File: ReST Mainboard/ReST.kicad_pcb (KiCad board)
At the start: 2 copper layers, 100 x 100 mm, 368 parts, among them P20 CONN_02X04, P21 CONN_02X04, P24 CONN_01X03, P26 CONN_01X03, P28 CONN_01X03, P30 CONN_01X03, P32 CONN_01X03, P34 CONN_01X03, P35 SCREW_01X04, P36 SCREW_01X04, P37 SCREW_01X04, P38 SCREW_01X04, P5 USB_OTG, P9 CONN_01X02, U2 USBLC6-2, U4 LM2574N-ADJ

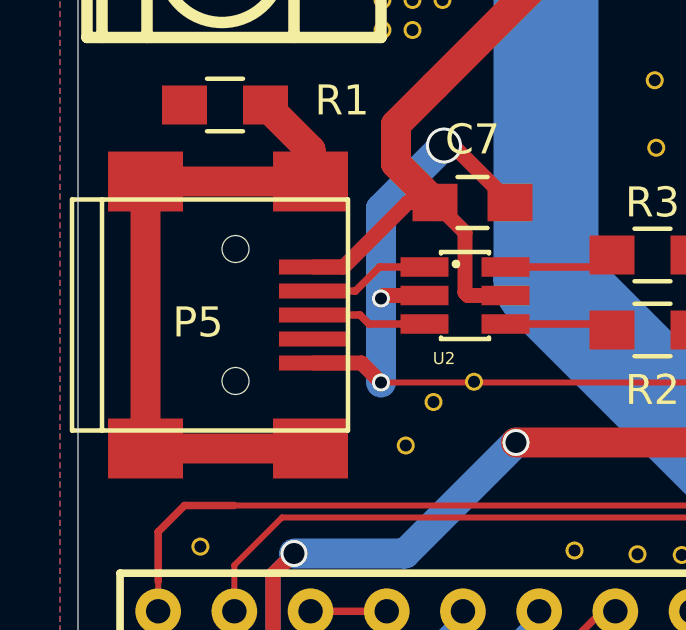
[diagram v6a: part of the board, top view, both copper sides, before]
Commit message: Finished Combined PCB and Gerber files
Combined pcb fits on 10x10cm, breakable and gerbers are finished for elecrow order. will order everything this weekend, lets see if it works.
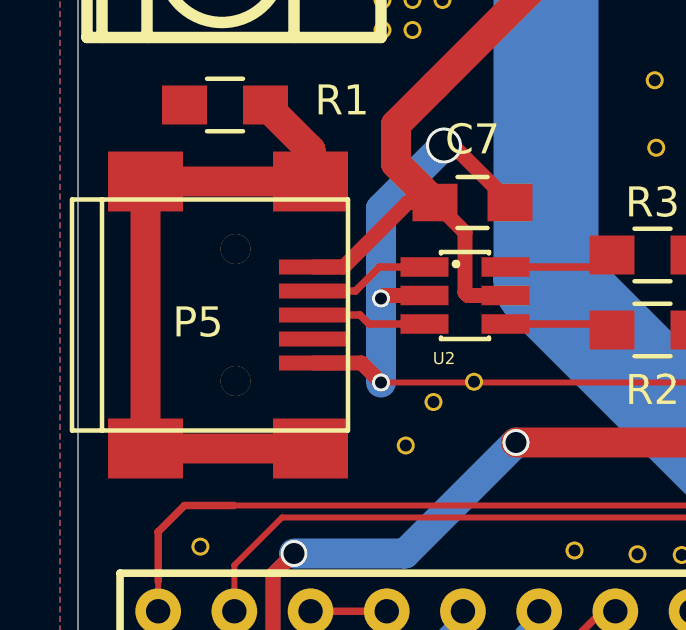
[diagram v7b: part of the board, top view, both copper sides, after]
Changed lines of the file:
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@@
   )
   (setup
-    (last_trace_width 0.5)
+    (last_trace_width 0.25)
     (user_trace_width 0.2)
     (user_trace_width 0.3)
@@
     (mod_text_size 1 1)
     (mod_text_width 0.15)
-    (pad_size 0.6 0.6)
-    (pad_drill 0.4)
+    (pad_size 1 1)
+    (pad_drill 1)
     (pad_to_mask_clearance 0.2)
     (aux_axis_origin 0 0)
@@
     (visible_elements 7FFFFF7F)
     (pcbplotparams
-      (layerselection 0x010f0_80000001)
+      (layerselection 0x000f0_80000001)
       (usegerberextensions true)
-      (excludeedgelayer true)
+      (usegerberattributes true)
+      (excludeedgelayer false)
       (linewidth 0.100000)
       (plotframeref false)
@@
     (pad 6 smd rect (at -2.14884 4.45008) (size 2.49936 1.99898) (layers F.Cu F.Paste F.Mask)
       (net 118 "Net-(P5-Pad6)"))
-    (pad "" np_thru_hole circle (at 0.8509 -2.19964) (size 0.89916 0.89916) (drill 0.89916) (layers *.Cu *.Mask F.SilkS))
-    (pad "" np_thru_hole circle (at 0.8509 2.19964) (size 0.89916 0.89916) (drill 0.89916) (layers *.Cu *.Mask F.SilkS))
+    (pad "" thru_hole circle (at 0.8509 -2.19964) (size 1 1) (drill 1) (layers *.Cu *.Mask F.SilkS))
+    (pad "" thru_hole circle (at 0.8509 2.19964) (size 1 1) (drill 1) (layers *.Cu *.Mask F.SilkS))
     (model ../../../../../../Users/Matjas/Documents/Git/RepRapSTM32duinoDriver/3D-Models/conn_pc/usb_B_mini_smd.wrl
       (at (xyz -0.025 0 0))

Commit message: Mainboard structure made and most modules finished
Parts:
- removed ?: , Pin_Headers:Pin_Header_Straight_1x04
- removed GND (x3), REF**11, REF**111 (x3), REF**11101, REF**1111 (x2), REF**11111 (x2), REF**111111, REF**111112, REF**111113, REF**111114, REF**111115, REF**111116, REF**11112, REF**111121, REF**111122, REF**111123, REF**111124, REF**111125, REF**111126, REF**11113, REF**111131, REF**111132, REF**111133, REF**111134, REF**111135, REF**111136, REF**11114, REF**111141, REF**111142, REF**111143, REF**111144, REF**111145, REF**111146, REF**11115, REF**111151, REF**111152, REF**111153, REF**111154, REF**111155, REF**111156, REF**11116, REF**1112, REF**11121 (x2), REF**11122, REF**11123, REF**11124, REF**11125, REF**11126, REF**1113, REF**1114, REF**1115, REF**1116, REF**112 (x2), REF**1121 (x2), REF**1122, REF**1123, REF**1124, REF**1125, REF**1126, REF**113 (x2), REF**1131 (x2), REF**1132, REF**1133, REF**1134, REF**1135, REF**1136, REF**114 (x2), REF**1141, REF**115 (x2), REF**1151, REF**116 (x2), REF**1161, REF**1171, REF**1181, REF**1191, REF**12, REF**121 (x3), REF**122 (x2), REF**123 (x2), REF**124 (x2), REF**125 (x2), REF**126 (x2), REF**131 (x5), REF**131111 (x6), REF**131112, REF**131113, REF**131114, REF**131115, REF**131121, REF**131122, REF**131123, REF**131124, REF**131125, REF**131131, REF**131132, REF**131133, REF**131134, REF**131135, REF**131141, REF**131142, REF**131143, REF**131144, REF**131145, REF**131151, REF**131152, REF**131153, REF**131154, REF**131155, REF**132 (x2), REF**133 (x2), REF**134 (x2), REF**135 (x2), REF**136, REF**141 (x2), REF**142, REF**143, REF**144, REF**145, REF**146, REF**21, REF**22, REF**31 (x58), REF**311 (x3), REF**3111 (x3), REF**3112 (x2), REF**3113, REF**312 (x3), REF**3121 (x3), REF**3122 (x2), REF**313 (x10), REF**3131 (x2), REF**3132, REF**3141 (x2), REF**3142, REF**3151 (x2), REF**3152, REF**3161, REF**32, REF**321 (x3), REF**322 (x3), REF**323 (x3), REF**331 (x2), REF**332 (x3), REF**333 (x3), REF**341, REF**342, REF**343: VIA-0.6mm, ReST-Library:VIA-0.6mm
- removed GND: , ReST-Library:VIA-0.6mm
- removed P20: CONN_02X04, ReST-Library:Pin_Header_Angled_2x04
- removed P22: , Pin_Headers:Pin_Header_Straight_1x03
- removed P25: , 2:mpt_0,5%2f6-2,54
- removed P26, P30, P32: CONN_01X03, Pin_Headers:Pin_Header_Straight_1x03
- removed R6: 2K7, Resistors_SMD:R_0805_HandSoldering
- removed R7: 1K6, Resistors_SMD:R_0805_HandSoldering
- added P11: CONN_01X04, Pin_Headers:Pin_Header_Straight_1x04, F.Cu at (197.2, 106.8)
- C1, C2, C3, C4, C5, C6, C9: value (none) -> 100nF
- C12: value 22uF -> 10uF; footprint ReST-Library:CP-PANASONIC-SMT_D -> Capacitors_SMD:C_0805_HandSoldering
- C13: value 220uF -> 10uF; footprint ReST-Library:CP-PANASONIC-SMT_D -> Capacitors_SMD:C_0805_HandSoldering
- C14, C15, C16, C17, C18, C19: value (none) -> 10nF
- C24, C25: value (none) -> 30pF
- C7: footprint Capacitors_SMD:C_0805_HandSoldering -> Capacitors_SMD:C_0603_HandSoldering
- C8: value (none) -> 10uF
- D1: value 1N5819 -> 1N400x; footprint ReST-Library:DO-214AC(SMA) -> ReST-Library:DO-214AC.SMA
- F1: footprint ReST-Library:JEF-703C -> ReST-Library:MINI-FUSE
- IC1: value (none) -> AT24C128
- L1: value (none) -> BEAD
- L2: value 330uH -> 2.2uH; footprint Inductors:SELF-WE-PD-XXL -> ReST-Library:CD32
- P1, P2: value (none) -> CONN_01X03; footprint ReST-Library:Pin_Header_Angled_2x08 -> Pin_Headers:Pin_Header_Straight_1x03
- P10, P19, P40, P41, P42: value (none) -> CONN_01X04
- P12: value (none) -> CONN_02X03; footprint Pin_Headers:Pin_Header_Straight_2x04 -> Pin_Headers:Pin_Header_Straight_2x03
- P13: value (none) -> CONN_02X04; footprint Pin_Headers:Pin_Header_Straight_1x03 -> ReST-Library:REST_STEPPER
- P14: value (none) -> CONN_02X03
- P15: value (none) -> CONN_02X04; footprint Pin_Headers:Pin_Header_Straight_1x05 -> ReST-Library:REST_STEPPER
- P16: value (none) -> CONN_02X06; footprint Pin_Headers:Pin_Header_Straight_1x03 -> ReST-Library:REST_ADDITIONAL
- P17: value (none) -> CONN_02X03; footprint Pin_Headers:Pin_Header_Straight_1x04 -> ReST-Library:REST_HEATBED
- P18, P39: value (none) -> CONN_02X04
- P23: value (none) -> CONN_02X07; footprint 2:mpt_0,5%2f6-2,54 -> ReST-Library:REST_HEATER
- P24: value CONN_01X03 -> CONN_02X07; footprint Pin_Headers:Pin_Header_Straight_1x03 -> ReST-Library:REST_HEATER
- P27: value (none) -> CONN_02X06; footprint 2:mpt_0,5%2f6-2,54 -> Pin_Headers:Pin_Header_Straight_2x06
- P3: value (none) -> CONN_01X03; footprint ReST-Library:Pin_Header_Angled_2x07 -> Pin_Headers:Pin_Header_Straight_1x03
- P35, P36, P37, P38: footprint 2:mpt_0,5%2f4-2,54 -> ReST-Library:pt_1,5-4-3,5-h
- P4: value (none) -> CONN_01X03; footprint ReST-Library:Pin_Header_Angled_2x10 -> Pin_Headers:Pin_Header_Straight_1x03
- P43, P44, P45, P46: value (none) -> CONN_02X03; footprint Pin_Headers:Pin_Header_Straight_2x03 -> ReST-Library:bb02-hp06
- P6, P7: value (none) -> CONN_02X05
- P8: value (none) -> CONN_01X03; footprint Pin_Headers:Pin_Header_Straight_1x09 -> Pin_Headers:Pin_Header_Straight_1x03
- P9: footprint 5mm-pitch-terminal:mkds_1,5-2 -> ReST-Library:screw-5-2P
- R10, R11, R8, R9: value (none) -> 100K
- R12, R13: value (none) -> 4K7
- R2, R3: footprint Resistors_SMD:R_0805_HandSoldering -> Resistors_SMD:R_0603_HandSoldering
- R5: value (none) -> 10K
- SW1: value (none) -> SW-SPST-NO
- U1: value (none) -> STM32F103VE; footprint Housings_QFP:TQFP-100_14x14mm_Pitch0.5mm -> ReST-Library:LQFP100-14x14
- U3: value (none) -> L7805ACD2T-TR
- U4: value LM2574N-ADJ -> LM3671MFX-3.3; footprint Housings_DIP:DIP-8_W7.62mm_LongPads -> TO_SOT_Packages_SMD:SOT-23-5
- U5, U6, U7, U8: value (none) -> POLOLU_A4988
- X1: value (none) -> Crystal_Small; footprint Crystals:Crystal_HC49-SD_SMD -> ReST-Library:2P-5032
- moved P2 197.0 mm to (191.3, 152.5), turned to 180 degrees
- moved P1 181.9 mm to (196.4, 152.5), turned to 180 degrees
- moved P3 161.6 mm to (193.8, 152.5), turned to 180 degrees
- moved P16 148.8 mm to (173.4, 144.7), turned to 180 degrees
- moved P4 148.1 mm to (188.7, 152.5), turned to 180 degrees
- moved P19 146.8 mm to (197.2, 110.2), turned to 270 degrees
- moved P10 142.7 mm to (197.2, 103.1), turned to 270 degrees
- moved P15 139.9 mm to (189.9, 71.5), turned to 0 degrees
- moved P6 137.1 mm to (197.2, 126.2), turned to 270 degrees
- moved P39 133.6 mm to (161.3, 141.7), turned to 270 degrees
- moved P7 130.2 mm to (197.2, 132.2), turned to 270 degrees
- moved P35 127.0 mm to (157.5, 149.7)
- moved P45 126.6 mm to (157.0, 126.3), turned to 90 degrees
- moved U7 126.3 mm to (157.5, 129.8), turned to 270 degrees
- moved R11 123.4 mm to (157.5, 131.6), turned to 180 degrees
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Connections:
- net Net-(C2-Pad2) renamed /RESET
- C10 pad 1: GND -> +12V
- C10 pad 2: +12V -> GND
- C11 pad 1: GND -> VEE
- C11 pad 2: VCC/2 -> GND
- C12 pad 1: VAA -> GND
- C12 pad 2: GND -> +5V
- C13 pad 1: +3V3 -> GND
- C13 pad 2: GND -> +3V3
- D1 pad 1: Net-(D1-Pad1) -> +12V
- L2 pad 1: Net-(D1-Pad1) -> Net-(L2-Pad1)
- P1 pad 1: +12V -> +3V3
- P1 pad 3: +12V -> /X-MIN
- P12 pad 1: +5V -> /SERVO1
- P12 pad 2: GND -> /SERVO2
- P12 pad 4: GND -> +5V
- P12 pad 5: +5V -> GND
- P13 pad 1: +12V -> /E1-STEP
- P13 pad 2: VAA -> /E1-EN
- P13 pad 3: +5V -> /E1-DIR
- P15 pad 1: GND -> /E2-STEP
- P15 pad 2: +3V3 -> /E2-EN
- P15 pad 3: /I2C-SCL -> /E2-DIR
- P15 pad 4: /I2C-SDA -> GND
- P15 pad 5: +5V -> +3V3
- P16 pad 1: VCC -> GND
- P16 pad 2: +5V -> GND
- P16 pad 3: VCC/2 -> GND
- P17 pad 2: GND -> +3V3
- P17 pad 3: /UART5-RX -> GND
- P17 pad 4: /UART5-TX -> /PWM-BED
- P2 pad 1: +12V -> +3V3
- P2 pad 3: +12V -> /Y-MIN
- P23 pad 1: /ENDSTOP_VCC -> +3V3
- P23 pad 2: GND -> +5V
- P23 pad 3: /X-MIN -> /T2
- P23 pad 4: /ENDSTOP_VCC -> /PWM-HEAT1
- P23 pad 5: GND -> +12V
- P23 pad 6: /X-MAX -> +12V
- P24 pad 1: /ENDSTOP_VCC -> +3V3
- P24 pad 2: GND -> +5V
- P24 pad 3: /X-MIN -> /T1
- P27 pad 1: /ENDSTOP_VCC -> /EXTRA0
- P27 pad 2: GND -> /EXTRA1
- P27 pad 3: /Z-MIN -> /EXTRA2
- P27 pad 4: /ENDSTOP_VCC -> /EXTRA3
- P27 pad 5: GND -> /EXTRA4
- P27 pad 6: /Z-MAX -> /EXTRA5
- P28 pad 1: /ENDSTOP_VCC -> +3V3
- P3 pad 1: +12V -> +3V3
- P3 pad 3: +12V -> /X-MAX
- P34 pad 1: /ENDSTOP_VCC -> +3V3
- P39 pad 1: Net-(P35-Pad4) -> Net-(P35-Pad1)
- P39 pad 2: Net-(P35-Pad4) -> Net-(P35-Pad1)
- P39 pad 3: Net-(P35-Pad3) -> Net-(P35-Pad2)
- P39 pad 4: Net-(P35-Pad3) -> Net-(P35-Pad2)
- P39 pad 5: Net-(P35-Pad2) -> Net-(P35-Pad3)
- P39 pad 6: Net-(P35-Pad2) -> Net-(P35-Pad3)
- P39 pad 7: Net-(P35-Pad1) -> Net-(P35-Pad4)
- P39 pad 8: Net-(P35-Pad1) -> Net-(P35-Pad4)
- P4 pad 1: +12V -> +3V3
- P4 pad 3: +12V -> /Y-MAX
- P40 pad 1: Net-(P36-Pad1) -> Net-(P36-Pad4)
- P40 pad 2: Net-(P36-Pad2) -> Net-(P36-Pad3)
- P40 pad 3: Net-(P36-Pad3) -> Net-(P36-Pad2)
- P40 pad 4: Net-(P36-Pad4) -> Net-(P36-Pad1)
- P41 pad 1: Net-(P37-Pad1) -> Net-(P37-Pad4)
- P41 pad 2: Net-(P37-Pad2) -> Net-(P37-Pad3)
- P41 pad 3: Net-(P37-Pad3) -> Net-(P37-Pad2)
- P41 pad 4: Net-(P37-Pad4) -> Net-(P37-Pad1)
- P42 pad 1: Net-(P38-Pad1) -> Net-(P38-Pad4)
- P42 pad 2: Net-(P38-Pad2) -> Net-(P38-Pad3)
- P42 pad 3: Net-(P38-Pad3) -> Net-(P38-Pad2)
- P42 pad 4: Net-(P38-Pad4) -> Net-(P38-Pad1)
- P8 pad 1: /EXTRA0 -> VEE
- P8 pad 2: /EXTRA1 -> +5V
- P8 pad 3: /EXTRA2 -> VCC
- U1 pad 59: /SERVO3 -> /EXTRA7
- U1 pad 60: /SERVO4 -> /EXTRA6
- U1 pad 80: /UART5-TX -> /EXTRA8
- U1 pad 81: (no net) -> /EXTRA11
- U1 pad 82: (no net) -> /EXTRA10
- U1 pad 83: /UART5-RX -> /EXTRA9
- U3 pad 3: VCC/2 -> VEE
- U4 pad 1: Net-(R6-Pad2) -> +5V
- U4 pad 2: (no net) -> GND
- U4 pad 3: GND -> +5V
- U4 pad 4: GND -> +3V3
- U4 pad 5: VAA -> Net-(L2-Pad1)
- U5 pad 3: Net-(P36-Pad4) -> Net-(P36-Pad1)
- U5 pad 4: Net-(P36-Pad3) -> Net-(P36-Pad2)
- U5 pad 5: Net-(P36-Pad2) -> Net-(P36-Pad3)
- U5 pad 6: Net-(P36-Pad1) -> Net-(P36-Pad4)
- U6 pad 3: Net-(P37-Pad4) -> Net-(P37-Pad1)
- U6 pad 4: Net-(P37-Pad3) -> Net-(P37-Pad2)
- U6 pad 5: Net-(P37-Pad2) -> Net-(P37-Pad3)
- U6 pad 6: Net-(P37-Pad1) -> Net-(P37-Pad4)
- U7 pad 3: Net-(P35-Pad4) -> Net-(P35-Pad1)
- U7 pad 4: Net-(P35-Pad3) -> Net-(P35-Pad2)
- U7 pad 5: Net-(P35-Pad2) -> Net-(P35-Pad3)
- U7 pad 6: Net-(P35-Pad1) -> Net-(P35-Pad4)
- U8 pad 3: Net-(P38-Pad4) -> Net-(P38-Pad1)
- U8 pad 4: Net-(P38-Pad3) -> Net-(P38-Pad2)
- U8 pad 5: Net-(P38-Pad2) -> Net-(P38-Pad3)
- U8 pad 6: Net-(P38-Pad1) -> Net-(P38-Pad4)
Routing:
- net +3V3: track 649.1 -> 5.56 mm, vias 33 -> 0
- net +12V: track 435.0 -> 0.00 mm, vias 6 -> 0
- net GND: track 332.2 -> 0.00 mm, vias 23 -> 0
- net +5V: track 318.0 -> 10.3 mm, vias 12 -> 0
- net /ENDSTOP_VCC: track 100.1 -> 0.00 mm
- net /PWM-BED: track 88.1 -> 0.00 mm, vias 3 -> 0
- net /Z-MAX: track 88.7 -> 3.14 mm, vias 1 -> 0
- net /PWM-ADD2: track 82.8 -> 0.00 mm, vias 3 -> 0
- net /T0: track 82.6 -> 0.00 mm, vias 3 -> 0
- net /PWM-ADD1: track 79.5 -> 0.00 mm, vias 3 -> 0
- net /PWM-ADD3: track 74.3 -> 0.00 mm, vias 3 -> 0
- net /Z-MIN: track 72.1 -> 3.02 mm, vias 1 -> 0
- net /PWM-ADD0: track 68.9 -> 0.00 mm, vias 1 -> 0
- net /PWM-HEAT0: track 65.6 -> 0.00 mm, vias 2 -> 0
- net /T1: track 64.4 -> 0.00 mm, vias 1 -> 0
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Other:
- board outline removed
- board text removed: "@maker_berry"
- board text removed: "ReST32 Main Rev. A | TEST"
